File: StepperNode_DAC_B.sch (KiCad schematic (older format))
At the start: 9 parts

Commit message: Update DAC's and routed gimbal position to MCU direct.
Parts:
- removed C? (x6): 0.1uF, symbol C
- removed U?: AMC7812, symbol AMC7812
- added C? (x6): C_100nF_50V, RLOOP_FOOTPRINTS:rLoop_C_0603, symbol C_100nF_50V
- added U?: AMC7812BSPAP, RLOOP_FOOTPRINTS:rLoop_PQFP64_10x10mm, symbol AMC7812BSPAP
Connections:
- net labels removed: BRAKE1_MLP, BRAKE2_MLP
- wire segments 39 -> 37

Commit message: First Revision -
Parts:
- removed C?: 4.7UF, symbol C
- removed R?: 10K, symbol R
- added C39: C_4u7_25V, RLOOP_FOOTPRINTS:rLoop_C_0805, symbol C_4u7_25V
- added R18: 10K, RLOOP_FOOTPRINTS:rLoop_R_0603, symbol 10K
- gave numbers to parts that had none: 7
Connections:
- net labels added: +3V3_B, +5V_B
- net labels removed: +3.3V, +5VA

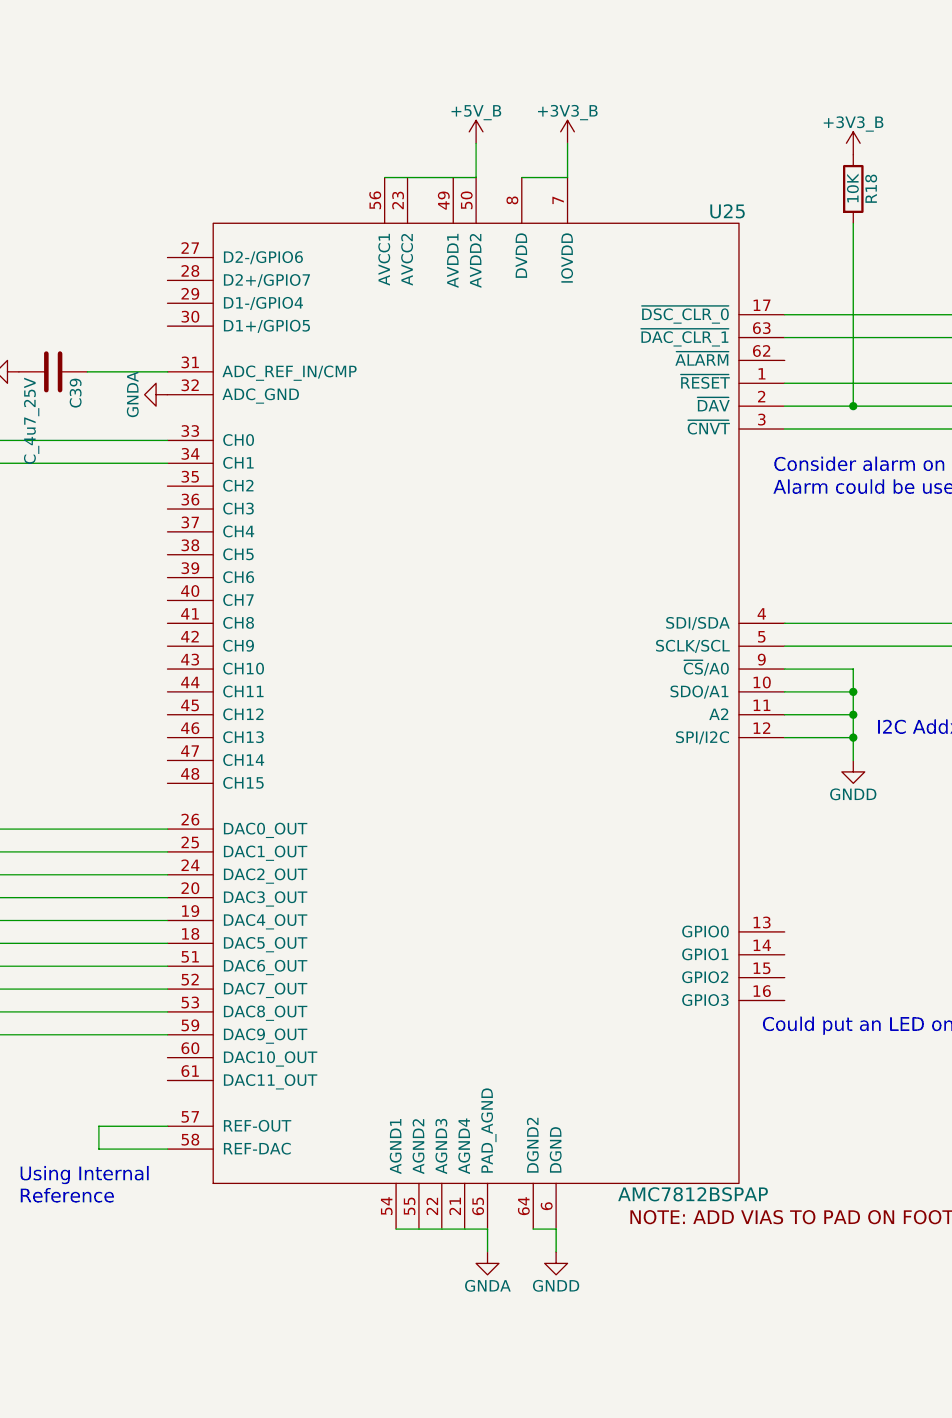
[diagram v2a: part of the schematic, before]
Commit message: Fix most ERC warnings (non-connected pins, etc)
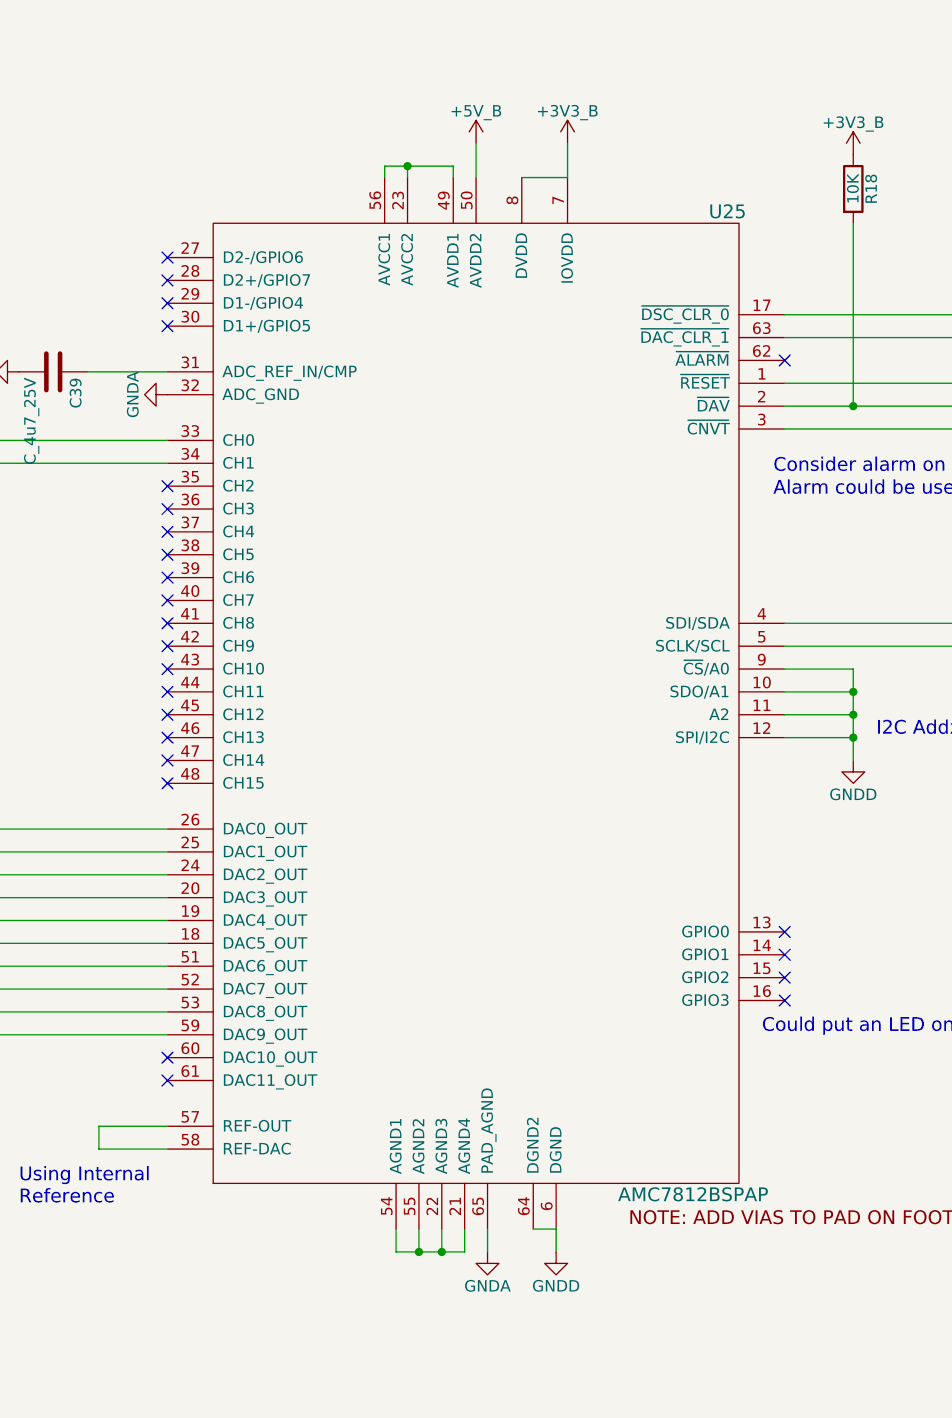
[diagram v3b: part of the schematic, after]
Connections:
- net +5V: no longer U25.56 (AVCC1)
- net GNDA: no longer U25.54 (AGND1)
- net at U25.21 (AGND4): now also U25.22 (AGND3), U25.54 (AGND1), U25.55 (AGND2)
- net at U25.23 (AVCC2): now also U25.49 (AVDD1), U25.56 (AVCC1)
- no-connect marks 0 -> 25
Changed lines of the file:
@@
 	9650 5150 10750 5150
 $Comp
-L GNDD #PWR182
+L GNDD #PWR0174
 U 1 1 5756580D
 P 9950 5650
-F 0 "#PWR182" H 9950 5400 50  0001 C CNN
+F 0 "#PWR0174" H 9950 5400 50  0001 C CNN
 F 1 "GNDD" H 9950 5500 50  0000 C CNN
 F 2 "" H 9950 5650 50  0000 C CNN
@@
 I2C Addx = 0xC2,0xC3
 $Comp
-L GNDD #PWR179
+L GNDD #PWR0175
 U 1 1 57565842
 P 8650 7800
-F 0 "#PWR179" H 8650 7550 50  0001 C CNN
+F 0 "#PWR0175" H 8650 7550 50  0001 C CNN
 F 1 "GNDD" H 8650 7650 50  0000 C CNN
 F 2 "" H 8650 7800 50  0000 C CNN
@@
 	6600 3950 6950 3950
 $Comp
-L GNDA #PWR176
+L GNDA #PWR0176
 U 1 1 57565852
 P 8350 7800
-F 0 "#PWR176" H 8350 7550 50  0001 C CNN
+F 0 "#PWR0176" H 8350 7550 50  0001 C CNN
 F 1 "GNDA" H 8350 7650 50  0000 C CNN
 F 2 "" H 8350 7800 50  0000 C CNN
@@
 $EndComp
 $Comp
-L GNDA #PWR168
+L GNDA #PWR0177
 U 1 1 57565858
 P 6950 4050
-F 0 "#PWR168" H 6950 3800 50  0001 C CNN
+F 0 "#PWR0177" H 6950 3800 50  0001 C CNN
 F 1 "GNDA" H 6950 3900 50  0000 C CNN
 F 2 "" H 6950 4050 50  0000 C CNN
@@
 $EndComp
 Wire Wire Line
-	7950 7700 8350 7700
-Wire Wire Line
 	8350 7700 8350 7800
 Wire Wire Line
 	8300 2950 8300 3100
 Wire Wire Line
-	8300 3100 7900 3100
-Wire Wire Line
 	8700 2950 8700 3100
 Wire Wire Line
 	8700 3100 8500 3100
 $Comp
-L GNDA #PWR163
+L GNDA #PWR0178
 U 1 1 57565876
 P 6300 3950
-F 0 "#PWR163" H 6300 3700 50  0001 C CNN
+F 0 "#PWR0178" H 6300 3700 50  0001 C CNN
 F 1 "GNDA" H 6300 3800 50  0000 C CNN
 F 2 "" H 6300 3950 50  0000 C CNN
@@
 Could put an LED on this for debug
 $Comp
-L GNDA #PWR165
+L GNDA #PWR0179
 U 1 1 575CA01E
 P 6350 1600
-F 0 "#PWR165" H 6350 1350 50  0001 C CNN
+F 0 "#PWR0179" H 6350 1350 50  0001 C CNN
 F 1 "GNDA" H 6350 1450 50  0000 C CNN
 F 2 "" H 6350 1600 50  0000 C CNN
@@
 $EndComp
 $Comp
-L GNDA #PWR167
+L GNDA #PWR0180
 U 1 1 575CA02A
 P 6750 1600
-F 0 "#PWR167" H 6750 1350 50  0001 C CNN
+F 0 "#PWR0180" H 6750 1350 50  0001 C CNN
 F 1 "GNDA" H 6750 1450 50  0000 C CNN
 F 2 "" H 6750 1600 50  0000 C CNN
@@
 $EndComp
 $Comp
-L GNDA #PWR170
+L GNDA #PWR0181
 U 1 1 575CA036
 P 7100 1600
-F 0 "#PWR170" H 7100 1350 50  0001 C CNN
+F 0 "#PWR0181" H 7100 1350 50  0001 C CNN
 F 1 "GNDA" H 7100 1450 50  0000 C CNN
 F 2 "" H 7100 1600 50  0000 C CNN
@@
 $EndComp
 $Comp
-L GNDA #PWR172
+L GNDA #PWR0182
 U 1 1 575CA042
 P 7500 1600
-F 0 "#PWR172" H 7500 1350 50  0001 C CNN
+F 0 "#PWR0182" H 7500 1350 50  0001 C CNN
 F 1 "GNDA" H 7500 1450 50  0000 C CNN
 F 2 "" H 7500 1600 50  0000 C CNN
@@
 $EndComp
 $Comp
-L GNDD #PWR174
+L GNDD #PWR0183
 U 1 1 575CA04E
 P 8000 1600
-F 0 "#PWR174" H 8000 1350 50  0001 C CNN
+F 0 "#PWR0183" H 8000 1350 50  0001 C CNN
 F 1 "GNDD" H 8000 1450 50  0000 C CNN
 F 2 "" H 8000 1600 50  0000 C CNN
@@
 $EndComp
 $Comp
-L GNDD #PWR178
+L GNDD #PWR0184
 U 1 1 575CA05A
 P 8400 1600
-F 0 "#PWR178" H 8400 1350 50  0001 C CNN
+F 0 "#PWR0184" H 8400 1350 50  0001 C CNN
 F 1 "GNDD" H 8400 1450 50  0000 C CNN
 F 2 "" H 8400 1600 50  0000 C CNN
@@
 $EndComp
 $Comp
-L +3V3_B #PWR181
+L +3V3_B #PWR0185
 U 1 1 5766B37C
 P 9950 3000
-F 0 "#PWR181" H 9950 2850 50  0001 C CNN
+F 0 "#PWR0185" H 9950 2850 50  0001 C CNN
 F 1 "+3V3_B" H 9950 3140 50  0000 C CNN
 F 2 "" H 9950 3000 60  0000 C CNN
@@
 $EndComp
 $Comp
-L +3V3_B #PWR180
+L +3V3_B #PWR0186
 U 1 1 5766B3A0
 P 8700 2950
-F 0 "#PWR180" H 8700 2800 50  0001 C CNN
+F 0 "#PWR0186" H 8700 2800 50  0001 C CNN
 F 1 "+3V3_B" H 8700 3090 50  0000 C CNN
 F 2 "" H 8700 2950 60  0000 C CNN
@@
 $EndComp
 $Comp
-L +3V3_B #PWR177
+L +3V3_B #PWR0187
 U 1 1 5766B3C7
 P 8400 1300
-F 0 "#PWR177" H 8400 1150 50  0001 C CNN
+F 0 "#PWR0187" H 8400 1150 50  0001 C CNN
 F 1 "+3V3_B" H 8400 1440 50  0000 C CNN
 F 2 "" H 8400 1300 60  0000 C CNN
@@
 $EndComp
 $Comp
-L +3V3_B #PWR173
+L +3V3_B #PWR0188
 U 1 1 5766B3D8
 P 8000 1300
-F 0 "#PWR173" H 8000 1150 50  0001 C CNN
+F 0 "#PWR0188" H 8000 1150 50  0001 C CNN
 F 1 "+3V3_B" H 8000 1440 50  0000 C CNN
 F 2 "" H 8000 1300 60  0000 C CNN
@@
 $EndComp
 $Comp
-L +5V_B #PWR175
+L +5V_B #PWR0189
 U 1 1 5766BBD3
 P 8300 2950
-F 0 "#PWR175" H 8300 2800 50  0001 C CNN
+F 0 "#PWR0189" H 8300 2800 50  0001 C CNN
 F 1 "+5V_B" H 8300 3090 50  0000 C CNN
 F 2 "" H 8300 2950 60  0000 C CNN
@@
 $EndComp
 $Comp
-L +5V_B #PWR171
+L +5V_B #PWR0190
 U 1 1 5766BCAE
 P 7500 1300
-F 0 "#PWR171" H 7500 1150 50  0001 C CNN
+F 0 "#PWR0190" H 7500 1150 50  0001 C CNN
 F 1 "+5V_B" H 7500 1440 50  0000 C CNN
 F 2 "" H 7500 1300 60  0000 C CNN
@@
 $EndComp
 $Comp
-L +5V_B #PWR169
+L +5V_B #PWR0191
 U 1 1 5766BCBF
 P 7100 1300
-F 0 "#PWR169" H 7100 1150 50  0001 C CNN
+F 0 "#PWR0191" H 7100 1150 50  0001 C CNN
 F 1 "+5V_B" H 7100 1440 50  0000 C CNN
 F 2 "" H 7100 1300 60  0000 C CNN
@@
 $EndComp
 $Comp
-L +5V_B #PWR166
+L +5V_B #PWR0192
 U 1 1 5766BCD0
 P 6750 1300
-F 0 "#PWR166" H 6750 1150 50  0001 C CNN
+F 0 "#PWR0192" H 6750 1150 50  0001 C CNN
 F 1 "+5V_B" H 6750 1440 50  0000 C CNN
 F 2 "" H 6750 1300 60  0000 C CNN
@@
 $EndComp
 $Comp
-L +5V_B #PWR164
+L +5V_B #PWR0193
 U 1 1 5766BCE1
 P 6350 1300
-F 0 "#PWR164" H 6350 1150 50  0001 C CNN
+F 0 "#PWR0193" H 6350 1150 50  0001 C CNN
 F 1 "+5V_B" H 6350 1440 50  0000 C CNN
 F 2 "" H 6350 1300 60  0000 C CNN
@@
 	1    0    0    -1
 $EndComp
+NoConn ~ 6950 3450
+NoConn ~ 6950 3550
+NoConn ~ 6950 3650
+NoConn ~ 6950 3750
+NoConn ~ 6950 4450
+NoConn ~ 6950 4550
+NoConn ~ 6950 4650
+NoConn ~ 6950 4750
+NoConn ~ 6950 4850
+NoConn ~ 6950 4950
+NoConn ~ 6950 5050
+NoConn ~ 6950 5150
+NoConn ~ 6950 5250
+NoConn ~ 6950 5350
+NoConn ~ 6950 5450
+NoConn ~ 6950 5550
+NoConn ~ 6950 5650
+NoConn ~ 6950 5750
+NoConn ~ 6950 6950
+NoConn ~ 6950 7050
+Wire Wire Line
+	7950 7700 7950 7800
+Wire Wire Line
+	7950 7800 8250 7800
+Wire Wire Line
+	8250 7800 8250 7700
+Wire Wire Line
+	8150 7700 8150 7800
+Connection ~ 8150 7800
+Wire Wire Line
+	8050 7700 8050 7800
+Connection ~ 8050 7800
+NoConn ~ 9650 6400
+NoConn ~ 9650 6500
+NoConn ~ 9650 6600
+NoConn ~ 9650 6700
+NoConn ~ 9650 3900
+Wire Wire Line
+	7900 3100 7900 3050
+Wire Wire Line
+	7900 3050 8200 3050
+Wire Wire Line
+	8200 3050 8200 3100
+Wire Wire Line
+	8000 3100 8000 3050
+Connection ~ 8000 3050
 $EndSCHEMATC
